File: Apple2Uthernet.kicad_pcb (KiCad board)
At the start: 2 copper layers, 79.8 x 69.8 mm, 71 parts, among them J1 Apple II Bus Card Edge, J2 RJ45_LED_Shielded, U1 74LS139, U2 74LS245, U3 W5100, U4 NCP1117-3.3_SOT223, U5 74LVC1G07, U6 74LVC1G17, U7 74LVC1G17, U8 74LVC1G17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

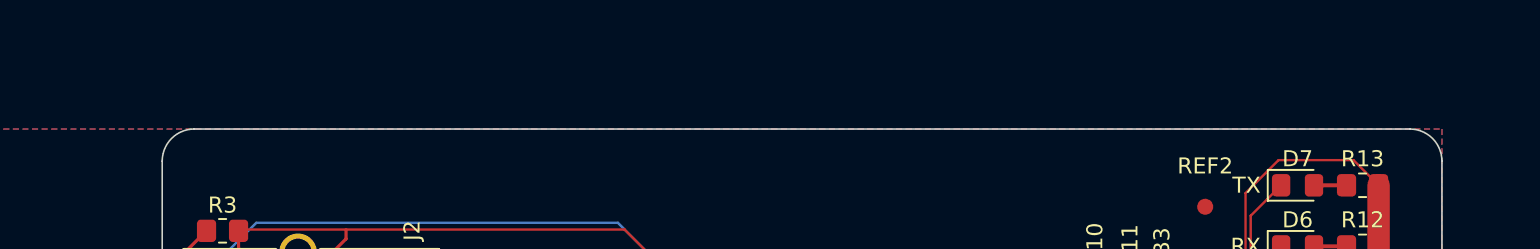
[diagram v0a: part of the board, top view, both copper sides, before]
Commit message: Make the board taller so that fiducial rails go on the left and right sides.
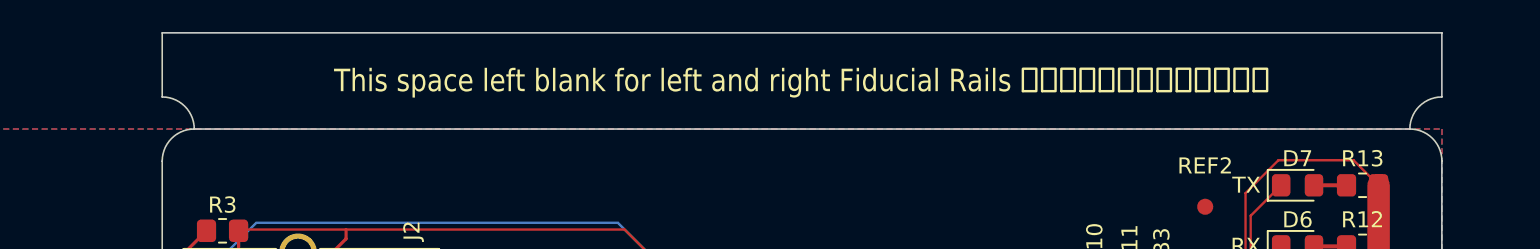
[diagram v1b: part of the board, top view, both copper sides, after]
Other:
- board size 79.8 x 69.8 mm -> 79.8 x 75.8 mm
- board text added: "This space left blank for left and right Fiducial Rails 此空间留空用于左右基准导轨"
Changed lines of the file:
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@@
     )
     (pad_to_mask_clearance 0)
-    (aux_axis_origin 104.8 140)
-    (grid_origin 104.8 140)
+    (aux_axis_origin 194.16 141.105)
+    (grid_origin 194.16 141.105)
     (pcbplotparams
       (layerselection 0x00010fc_ffffffff)
@@
   (gr_line (start 271 132.215) (end 271 99.005) (layer "Cmts.User") (width 0.15))
   (gr_line (start 255.661 128.016) (end 251.14 128.016) (layer "Edge.Cuts") (width 0.1))
+  (gr_line (start 274 56.365) (end 194.16 56.365) (layer "Edge.Cuts") (width 0.1))
+  (gr_line (start 274 60.365) (end 274 56.365) (layer "Edge.Cuts") (width 0.1))
   (gr_arc (start 243.52 106.625) (mid 251.304144 101.11589) (end 260.604 99.005) (layer "Edge.Cuts") (width 0.1))
   (gr_line (start 272 62.365) (end 196.16 62.365) (layer "Edge.Cuts") (width 0.1))
@@
   (gr_line (start 251.14 128.016) (end 243.52 120.396) (layer "Edge.Cuts") (width 0.1))
   (gr_arc (start 194.16 64.365) (mid 194.745786 62.950786) (end 196.16 62.365) (layer "Edge.Cuts") (width 0.1))
+  (gr_arc (start 194.16 60.365) (mid 195.574214 60.950786) (end 196.16 62.365) (layer "Edge.Cuts") (width 0.1))
   (gr_arc (start 272 62.365) (mid 273.414214 62.950786) (end 274 64.365) (layer "Edge.Cuts") (width 0.1))
   (gr_arc (start 274 94.805) (mid 272.769848 97.774848) (end 269.8 99.005) (layer "Edge.Cuts") (width 0.1))
   (gr_arc (start 243.52 120.396) (mid 241.013883 113.5105) (end 243.52 106.625) (layer "Edge.Cuts") (width 0.1))
+  (gr_arc (start 272 62.365) (mid 272.585786 60.950786) (end 274 60.365) (layer "Edge.Cuts") (width 0.1))
+  (gr_line (start 194.16 60.365) (end 194.16 56.365) (layer "Edge.Cuts") (width 0.1))
   (gr_line (start 260.604 101.545) (end 260.604 99.005) (layer "User.1") (width 0.1))
   (gr_line (start 194.16 132.215) (end 205.13 132.215) (layer "User.1") (width 0.01))
@@
   (gr_line (start 243.52 106.625) (end 251.14 106.625) (layer "User.1") (width 0.1))
   (gr_line (start 274 132.215) (end 274 145.55) (layer "User.1") (width 0.1))
+  (gr_line (start 160 141.105) (end 100 141.105) (layer "User.1") (width 0.001))
   (gr_line (start 174 132.215) (end 174 145.55) (layer "User.1") (width 0.1))
   (gr_line (start 210 128.865) (end 199.415 128.865) (layer "User.1") (width 0.01))
   (gr_line (start 194.66 132.215) (end 194.66 64.365) (layer "User.4") (width 0.1))
   (gr_line (start 273.5 132.215) (end 273.5 64.365) (layer "User.4") (width 0.1))
+  (gr_text "This space left blank for left and right Fiducial Rails 此空间留空用于左右基准导轨" (at 234.08 59.355) (layer "F.SilkS")
+    (effects (font (size 1.4 1.2) (thickness 0.15)))
+  )
   (gr_text "JLCJLCJLCJLC" (at 237.315 96.215) (layer "F.SilkS")
     (effects (font (size 0.8 0.8) (thickness 0.15)))
@@
       )
     )
+  )
+  (zone (net 0) (net_name "") (layers F&B.Cu *.Adhes *.Paste *.Mask "User.1") (name "BreakAway") (hatch edge 0.508)
+    (connect_pads (clearance 0))
+    (min_thickness 0.254)
+    (keepout (tracks not_allowed) (vias not_allowed) (pads not_allowed) (copperpour not_allowed) (footprints not_allowed))
+    (fill (thermal_gap 0.508) (thermal_bridge_width 0.508))
+    (polygon
+      (pts
+        (xy 274 62.365)
+        (xy 194.16 62.365)
+        (xy 194.16 56.365)
+        (xy 274 56.365)
+      )
+    )

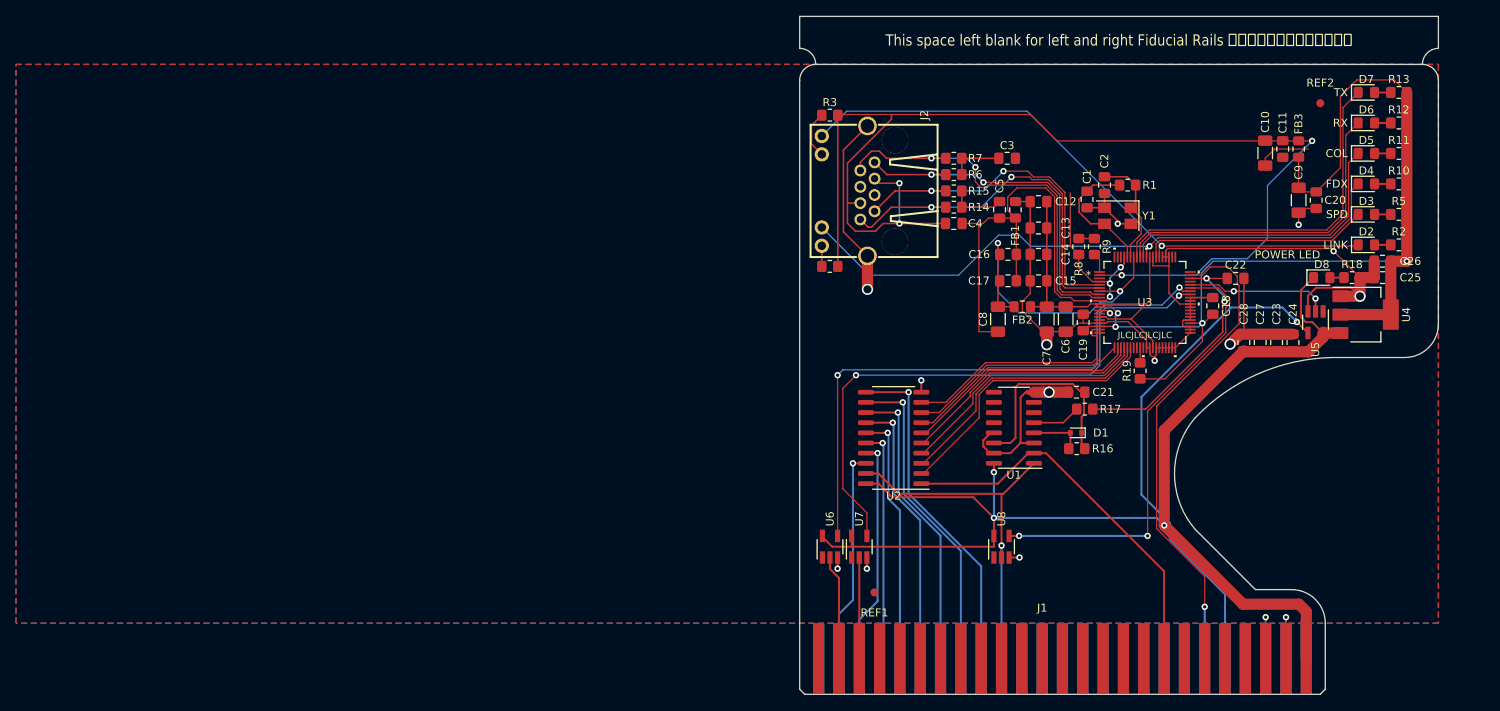
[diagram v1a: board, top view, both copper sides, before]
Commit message: Added Fiducial Rails on the Left and Right sides.
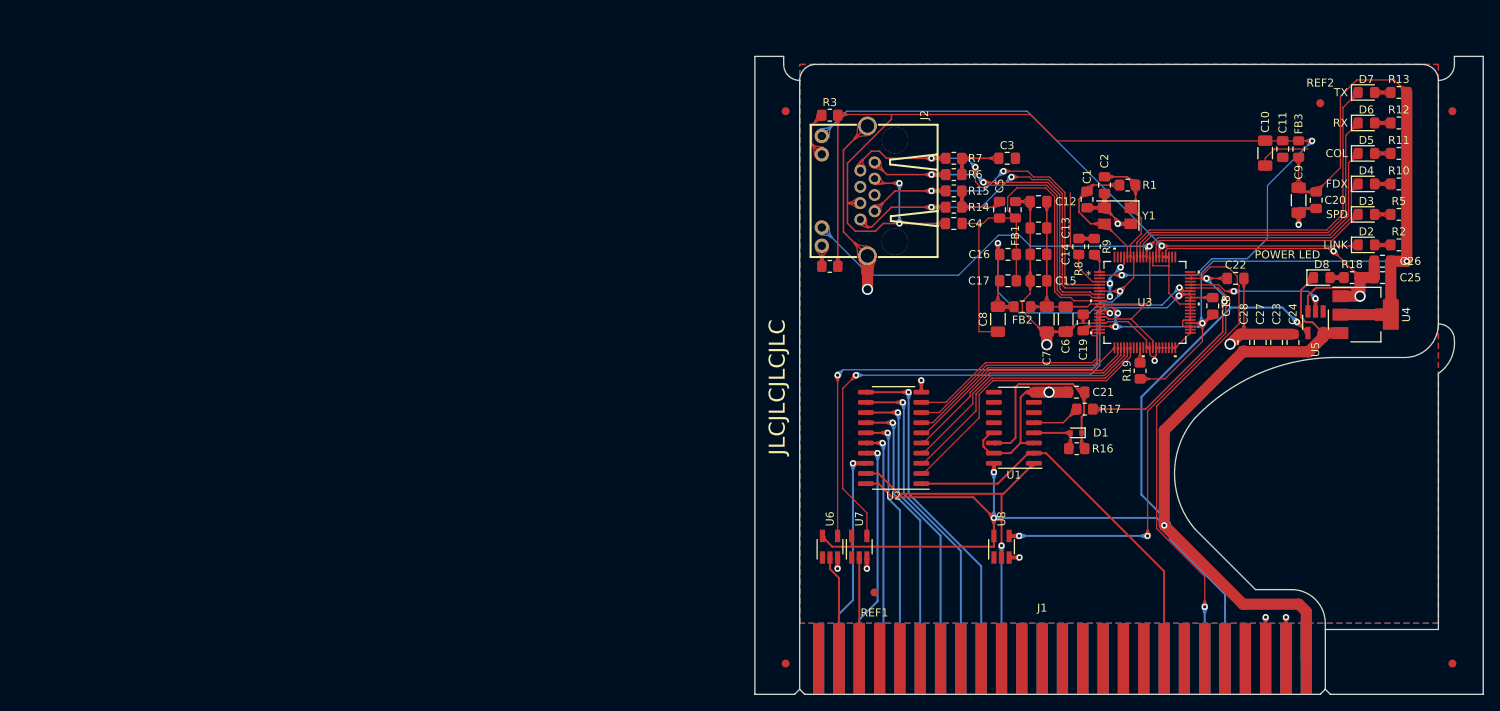
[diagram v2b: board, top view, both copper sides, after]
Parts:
- added REF**: Fiducial_1mm_Mask2mm, Fiducial:Fiducial_1mm_Mask2mm, F.Cu at (275.8, 68.2)
- added REF**: Fiducial_1mm_Mask2mm, Fiducial:Fiducial_1mm_Mask2mm, F.Cu at (192.4, 68.2)
- added REF**: Fiducial_1mm_Mask2mm, Fiducial:Fiducial_1mm_Mask2mm, F.Cu at (192.4, 137.3)
- added REF**: Fiducial_1mm_Mask2mm, Fiducial:Fiducial_1mm_Mask2mm, F.Cu at (275.8, 137.3)
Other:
- board size 79.8 x 75.8 mm -> 91 x 79.7 mm
- board text added: "BreakAway Rail Brace"
- board text removed: "This space left blank for left and right Fiducial Rails 此空间留空用于左右基准导轨"

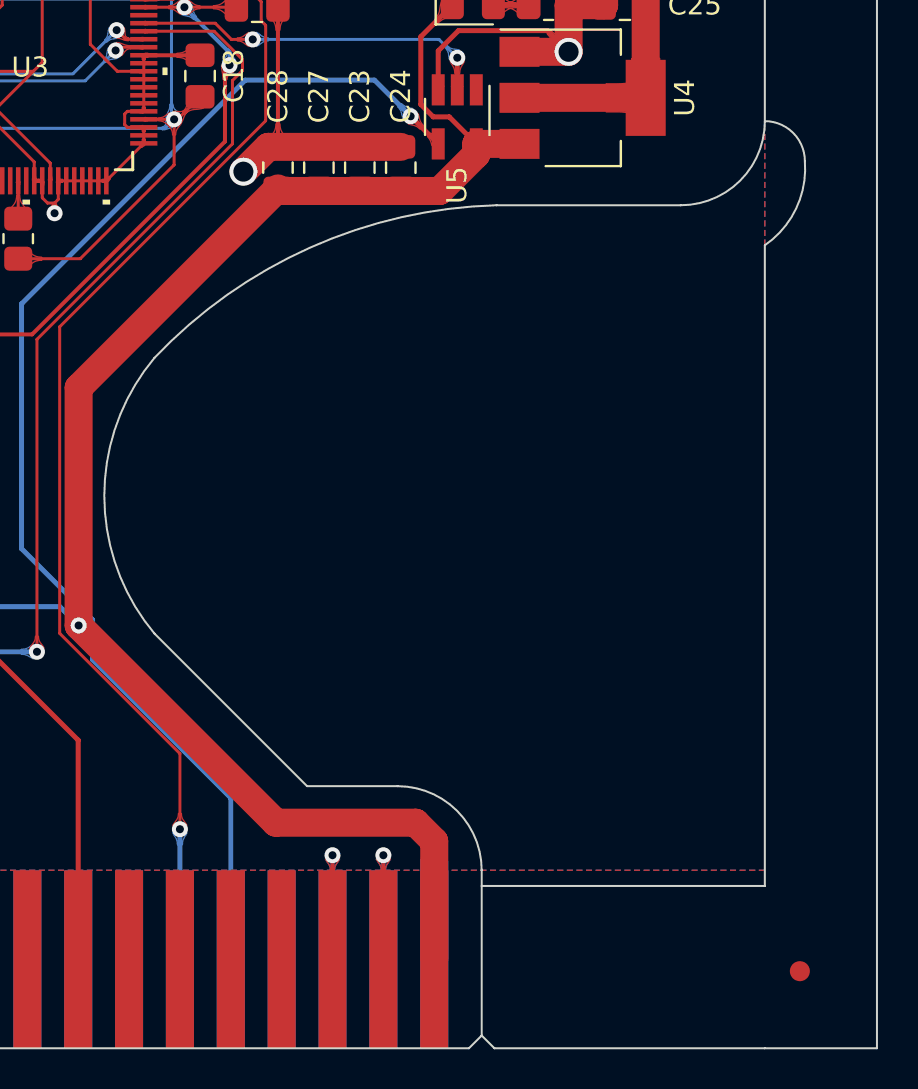
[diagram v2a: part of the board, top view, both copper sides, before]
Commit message: Updated Fiducial rails; Changed 1 resistor due to stocking issues.
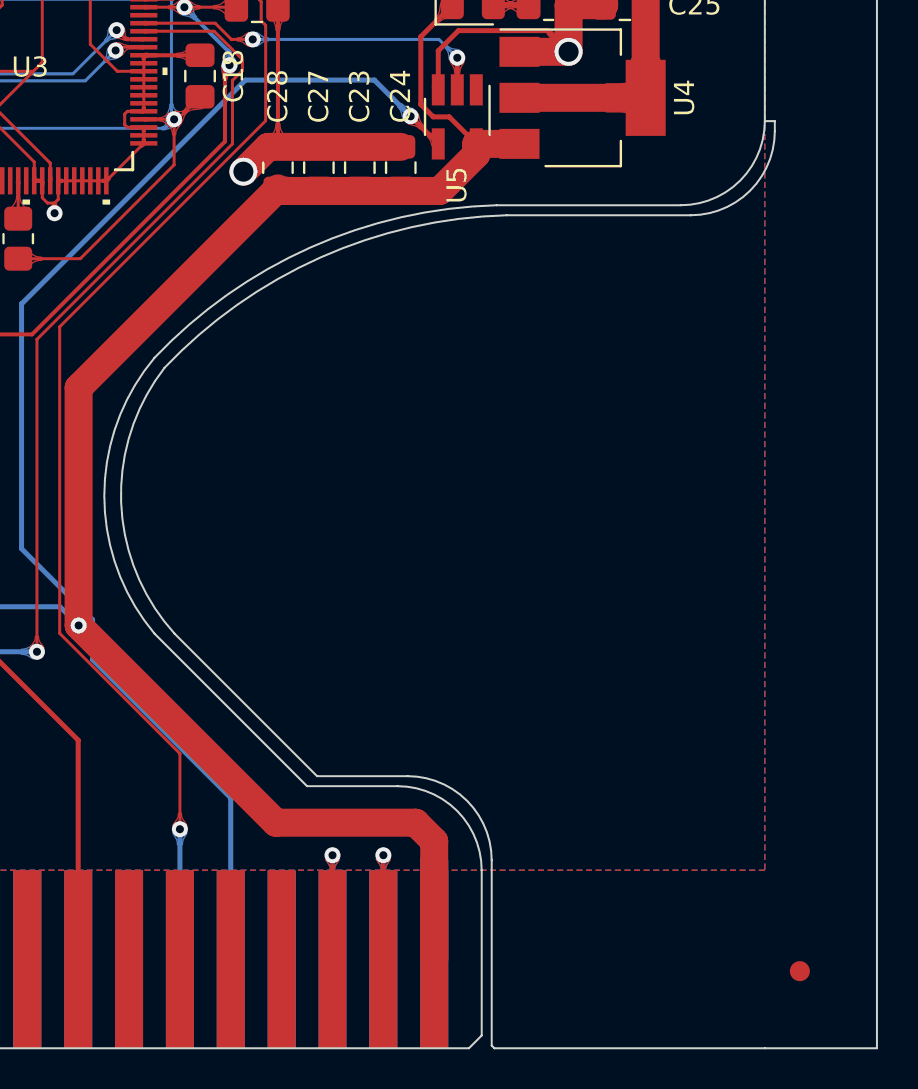
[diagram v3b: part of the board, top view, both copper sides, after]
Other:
- outline, holes or cut-outs redrawn
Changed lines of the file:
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@@
     (tags "resistor handsolder")
     (property "Description" "RES SMD 1.43K OHM 1% 1/8W 0805")
-    (property "LCSC" "C101474")
+    (property "LCSC" "C336837")
     (property "MPN" "ERJ-6ENF1431V")
     (property "Manufacturer" "Panasonic Electronic Components")
@@
     )
   )
-  (gr_line (start 259.86 132.215) (end 271 132.215) (layer "Cmts.User") (width 0.15))
-  (gr_line (start 271 132.215) (end 271 99.005) (layer "Cmts.User") (width 0.15))
   (gr_line (start 255.661 128.016) (end 251.14 128.016) (layer "Edge.Cuts") (width 0.1))
-  (gr_line (start 274 133) (end 274 101.005) (layer "Edge.Cuts") (width 0.1))
   (gr_line (start 276 61.365) (end 279.6 61.365) (layer "Edge.Cuts") (width 0.1))
   (gr_arc (start 243.52 106.625) (mid 251.304144 101.11589) (end 260.604 99.005) (layer "Edge.Cuts") (width 0.1))
+  (gr_line (start 274.5 94.805) (end 274.5 95.305) (layer "Edge.Cuts") (width 0.1))
   (gr_line (start 272 62.365) (end 196.16 62.365) (layer "Edge.Cuts") (width 0.1))
-  (gr_line (start 274 133) (end 259.86 133) (layer "Edge.Cuts") (width 0.1))
   (gr_line (start 194.16 140.47) (end 193.525 141.105) (layer "Edge.Cuts") (width 0.1))
   (gr_arc (start 255.661 128.016) (mid 258.630141 129.245859) (end 259.86 132.215) (layer "Edge.Cuts") (width 0.1))
-  (gr_arc (start 274 94.805) (mid 275.414214 95.390786) (end 276 96.805) (layer "Edge.Cuts") (width 0.1))
   (gr_line (start 274 94.805) (end 274 64.365) (layer "Edge.Cuts") (width 0.1))
   (gr_line (start 260.604 99.005) (end 269.8 99.005) (layer "Edge.Cuts") (width 0.1))
   (gr_line (start 188.56 61.365) (end 192.16 61.365) (layer "Edge.Cuts") (width 0.1))
   (gr_line (start 194.16 132.215) (end 194.16 64.365) (layer "Edge.Cuts") (width 0.1))
+  (gr_arc (start 274.5 95.305) (mid 273.269848 98.274848) (end 270.3 99.505) (layer "Edge.Cuts") (width 0.1))
+  (gr_arc (start 244.52 120.396) (mid 241.854871 113.851493) (end 244.02 107.125) (layer "Edge.Cuts") (width 0.1))
   (gr_line (start 274 141.105) (end 260.495 141.105) (layer "Edge.Cuts") (width 0.1))
   (gr_line (start 188.56 141.105) (end 193.525 141.105) (layer "Edge.Cuts") (width 0.1))
+  (gr_line (start 260.36 131.715) (end 260.36 140.97) (layer "Edge.Cuts") (width 0.1))
   (gr_line (start 274 141.105) (end 279.6 141.105) (layer "Edge.Cuts") (width 0.1))
+  (gr_line (start 261.104 99.505) (end 270.3 99.505) (layer "Edge.Cuts") (width 0.1))
   (gr_line (start 251.14 128.016) (end 243.52 120.396) (layer "Edge.Cuts") (width 0.1))
   (gr_arc (start 194.16 64.365) (mid 194.745786 62.950786) (end 196.16 62.365) (layer "Edge.Cuts") (width 0.1))
-  (gr_arc (start 276 96.805) (mid 275.562693 99.172949) (end 274 101.005) (layer "Edge.Cuts") (width 0.1))
+  (gr_line (start 251.64 127.516) (end 244.52 120.396) (layer "Edge.Cuts") (width 0.1))
   (gr_arc (start 272 62.365) (mid 273.414214 62.950786) (end 274 64.365) (layer "Edge.Cuts") (width 0.1))
   (gr_arc (start 274 94.805) (mid 272.769848 97.774848) (end 269.8 99.005) (layer "Edge.Cuts") (width 0.1))
   (gr_arc (start 243.52 120.396) (mid 241.013883 113.5105) (end 243.52 106.625) (layer "Edge.Cuts") (width 0.1))
+  (gr_line (start 274 94.805) (end 274.5 94.805) (layer "Edge.Cuts") (width 0.1))
   (gr_line (start 192.16 61.365) (end 192.16 62.365) (layer "Edge.Cuts") (width 0.1))
-  (gr_line (start 259.86 140.47) (end 260.495 141.105) (layer "Edge.Cuts") (width 0.1))
+  (gr_line (start 260.36 140.97) (end 260.495 141.105) (layer "Edge.Cuts") (width 0.1))
   (gr_line (start 276 62.365) (end 276 61.365) (layer "Edge.Cuts") (width 0.1))
   (gr_arc (start 194.16 64.365) (mid 192.745786 63.779214) (end 192.16 62.365) (layer "Edge.Cuts") (width 0.1))
   (gr_arc (start 276 62.365) (mid 275.414214 63.779214) (end 274 64.365) (layer "Edge.Cuts") (width 0.1))
+  (gr_line (start 256.161 127.516) (end 251.64 127.516) (layer "Edge.Cuts") (width 0.1))
   (gr_line (start 188.56 141.105) (end 188.56 61.365) (layer "Edge.Cuts") (width 0.1))
+  (gr_arc (start 256.161 127.516) (mid 259.130141 128.745859) (end 260.36 131.715) (layer "Edge.Cuts") (width 0.1))
+  (gr_arc (start 244.02 107.125) (mid 251.80414 101.615873) (end 261.104 99.505) (layer "Edge.Cuts") (width 0.1))
   (gr_line (start 279.6 141.105) (end 279.6 61.365) (layer "Edge.Cuts") (width 0.1))
-  (gr_line (start 260.604 101.545) (end 260.604 99.005) (layer "User.1") (width 0.1))
   (gr_line (start 194.16 132.215) (end 205.13 132.215) (layer "User.1") (width 0.01))
-  (gr_line (start 266.8 99.005) (end 271 99.005) (layer "User.1") (width 0.1))
-  (gr_line (start 255.661 128.016) (end 260.604 128.016) (layer "User.1") (width 0.1))
-  (gr_line (start 251.14 128.016) (end 251.14 120.396) (layer "User.1") (width 0.1))
-  (gr_line (start 251.14 106.625) (end 251.14 101.545) (layer "User.1") (width 0.1))
-  (gr_line (start 243.52 106.625) (end 243.52 120.396) (layer "User.1") (width 0.1))
-  (gr_line (start 243.52 120.396) (end 251.14 120.396) (layer "User.1") (width 0.1))
-  (gr_line (start 251.14 101.545) (end 260.604 101.545) (layer "User.1") (width 0.1))
-  (gr_line (start 260.604 128.016) (end 260.604 132.215) (layer "User.1") (width 0.1))
   (gr_line (start 194.16 127.215) (end 204.495 127.215) (layer "User.1") (width 0.1))
-  (gr_line (start 243.52 106.625) (end 251.14 106.625) (layer "User.1") (width 0.1))
   (gr_line (start 160 141.105) (end 100 141.105) (layer "User.1") (width 0.001))
   (gr_line (start 174 132.215) (end 174 145.55) (layer "User.1") (width 0.1))
   (gr_line (start 210 128.865) (end 199.415 128.865) (layer "User.1") (width 0.01))
   (gr_line (start 194.66 132.215) (end 194.66 64.365) (layer "User.4") (width 0.1))
-  (gr_line (start 273.5 132.215) (end 273.5 64.365) (layer "User.4") (width 0.1))
   (gr_text "JLCJLCJLCJLC" (at 191.36 102.735 90) (layer "F.SilkS")
     (effects (font (size 2 2) (thickness 0.5)))
